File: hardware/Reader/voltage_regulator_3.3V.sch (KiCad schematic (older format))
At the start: 8 parts

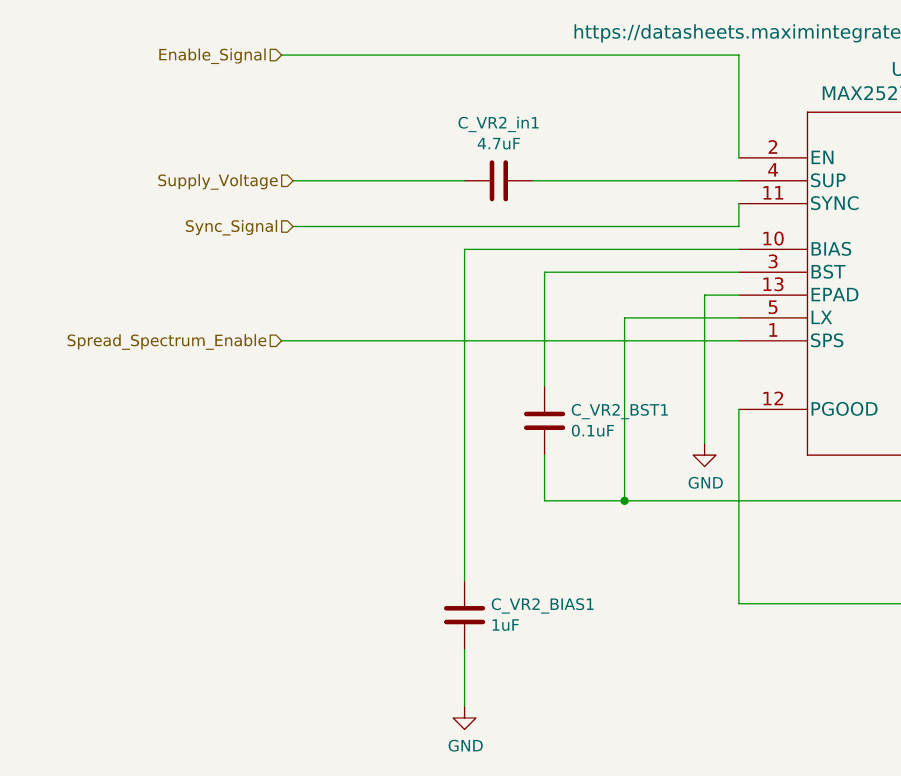
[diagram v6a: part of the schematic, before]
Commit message: Fixed bugs in schematic. Updated BOM list. Swapped to using ESP32 holder. Updated PCB layout to v0.0.2. Updated schematic to v0.0.4
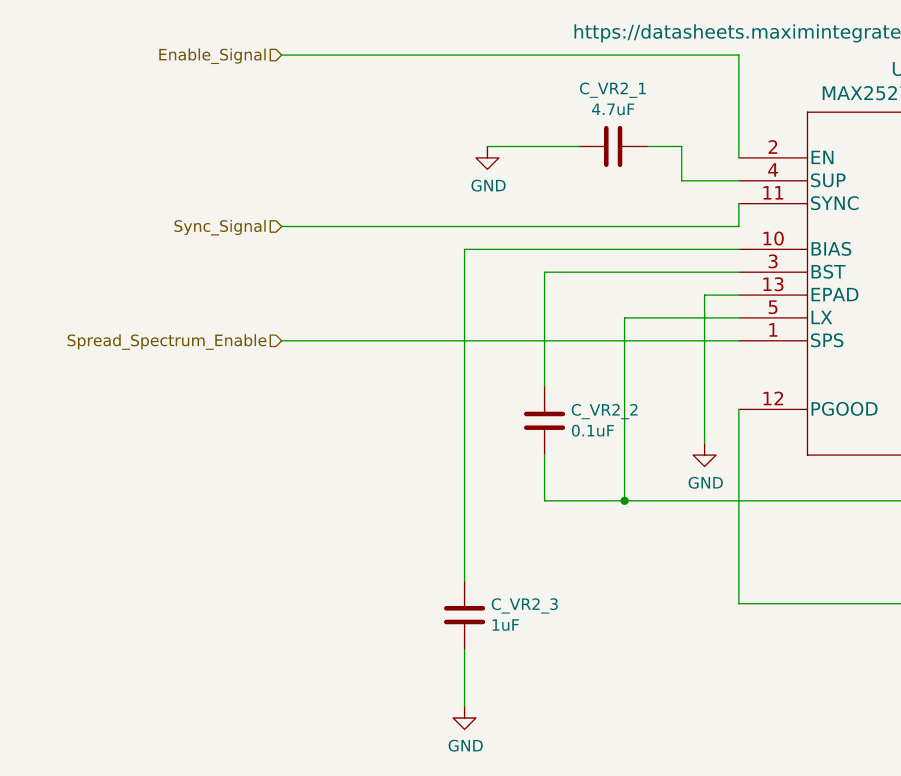
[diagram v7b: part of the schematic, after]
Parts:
- renumbered C_VR2_in1 to C_VR2_1, C_VR2_BST1 to C_VR2_2, C_VR2_BIAS1 to C_VR2_3
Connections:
- net Supply_Voltage is gone; now on net GND: C_VR2_1.2
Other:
- moved on the sheet: C_VR2_1
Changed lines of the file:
@@
 Sheet 19 19
 Title "CANnect Reader | Voltage Regulator (3.3V)"
-Date "2020-10-27"
-Rev "0.0.03"
+Date "2020-10-28"
+Rev "0.0.04"
 Comp "CANtech"
 Comment1 "Created by Choong Jin Ng | jin8383@gmail.com"
@@
 Text HLabel 2450 1850 0    50   Input ~ 0
 Enable_Signal
-Text HLabel 2500 2400 0    50   Input ~ 0
-Supply_Voltage
-Text HLabel 2500 2600 0    50   Input ~ 0
+Text HLabel 2450 2600 0    50   Input ~ 0
 Sync_Signal
 Text HLabel 9750 2400 2    50   Output ~ 0
@@
 L Device:C C_VR2_in?
 U 1 1 5FF3161F
-P 3400 2400
+P 3900 2250
 AR Path="/5F8ADA45/5F9EA8B0/5FF3161F" Ref="C_VR2_in?"  Part="1"
-AR Path="/5F8ADA45/5FF30350/5FF3161F" Ref="C_VR2_in1"  Part="1"
-F 0 "C_VR2_in1" V 3148 2400 50  0000 C CNN
-F 1 "4.7uF" V 3239 2400 50  0000 C CNN
-F 2 "footprints:C1206C475K3RACAUTO" H 3438 2250 50  0001 C CNN
-F 3 "https://api.kemet.com/component-edge/download/specsheet/C1206C475K3RACAUTO.pdf" H 3400 2400 50  0001 C CNN
-F 4 "C1206C475K3RACAUTO" H 3400 2400 50  0001 C CNN "Part Name"
-F 5 "Kermet" H 3400 2400 50  0001 C CNN "Manufacturer"
-F 6 "DigiKey Canada" H 3400 2400 50  0001 C CNN "Vendor"
-F 7 "399-7029-1-ND" H 3400 2400 50  0001 C CNN "digikeypn"
-	1    3400 2400
+AR Path="/5F8ADA45/5FF30350/5FF3161F" Ref="C_VR2_1"  Part="1"
+F 0 "C_VR2_1" V 3648 2250 50  0000 C CNN
+F 1 "4.7uF" V 3739 2250 50  0000 C CNN
+F 2 "footprints:C1206C475K3RACAUTO" H 3938 2100 50  0001 C CNN
+F 3 "https://api.kemet.com/component-edge/download/specsheet/C1206C475K3RACAUTO.pdf" H 3900 2250 50  0001 C CNN
+F 4 "C1206C475K3RACAUTO" H 3900 2250 50  0001 C CNN "Part Name"
+F 5 "Kermet" H 3900 2250 50  0001 C CNN "Manufacturer"
+F 6 "DigiKey Canada" H 3900 2250 50  0001 C CNN "Vendor"
+F 7 "399-7029-1-ND" H 3900 2250 50  0001 C CNN "digikeypn"
+	1    3900 2250
 	0    1    1    0
 $EndComp
@@
 	4450 1850 4450 2300
 Wire Wire Line
-	2500 2400 3250 2400
-Wire Wire Line
-	3550 2400 4450 2400
-Wire Wire Line
-	2500 2600 4450 2600
+	2450 2600 4450 2600
 Wire Wire Line
 	4450 2600 4450 2500
@@
 P 3600 3450
 AR Path="/5F8ADA45/5F9EA8B0/5FF31636" Ref="C_VR2_BST?"  Part="1"
-AR Path="/5F8ADA45/5FF30350/5FF31636" Ref="C_VR2_BST1"  Part="1"
-F 0 "C_VR2_BST1" H 3715 3496 50  0000 L CNN
+AR Path="/5F8ADA45/5FF30350/5FF31636" Ref="C_VR2_2"  Part="1"
+F 0 "C_VR2_2" H 3715 3496 50  0000 L CNN
 F 1 "0.1uF" H 3715 3405 50  0000 L CNN
 F 2 "footprints:CAPC1608X90" H 3638 3300 50  0001 C CNN
@@
 P 3250 4300
 AR Path="/5F8ADA45/5F9EA8B0/5FF31652" Ref="C_VR2_BIAS?"  Part="1"
-AR Path="/5F8ADA45/5FF30350/5FF31652" Ref="C_VR2_BIAS1"  Part="1"
-F 0 "C_VR2_BIAS1" H 3365 4346 50  0000 L CNN
+AR Path="/5F8ADA45/5FF30350/5FF31652" Ref="C_VR2_3"  Part="1"
+F 0 "C_VR2_3" H 3365 4346 50  0000 L CNN
 F 1 "1uF" H 3365 4255 50  0000 L CNN
 F 2 "footprints:0603" H 3288 4150 50  0001 C CNN
@@
 Wire Notes Line
 	8850 2600 8850 3650
+Wire Wire Line
+	4450 2400 4200 2400
+Wire Wire Line
+	4200 2400 4200 2250
+Wire Wire Line
+	4200 2250 4050 2250
+$Comp
+L power:GND #PWR0108
+U 1 1 5F99A55F
+P 3350 2250
+F 0 "#PWR0108" H 3350 2000 50  0001 C CNN
+F 1 "GND" H 3355 2077 50  0000 C CNN
+F 2 "" H 3350 2250 50  0001 C CNN
+F 3 "" H 3350 2250 50  0001 C CNN
+	1    3350 2250
+	1    0    0    -1
+$EndComp
+Wire Wire Line
+	3350 2250 3750 2250
 $EndSCHEMATC
